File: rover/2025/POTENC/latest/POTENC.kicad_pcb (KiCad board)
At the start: 4 copper layers, 20 x 23.1 mm, 4 parts, among them J1 POT, J2 Conn_01x06_Socket, J3 RJ50-SS-641010-A-NF-A111

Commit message: ARM-JL REV0 done
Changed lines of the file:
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@@
 	)
 	(segment
-		(start 54.28766 38.84)
-		(end 54.40766 38.84)
-		(width 0.1565)
-		(layer "F.Cu")
-		(net 5)
-	)
-	(segment
-		(start 54.04766 38.428531)
-		(end 54.04766 38.6)
-		(width 0.1565)
-		(layer "F.Cu")
-		(net 5)
-	)
-	(segment
-		(start 56.778149 38.84)
-		(end 56.901 38.84)
-		(width 0.1565)
-		(layer "F.Cu")
-		(net 5)
-	)
-	(segment
-		(start 53.68766 38.188531)
-		(end 53.80766 38.188531)
+		(start 54.432799 38.84)
+		(end 55.237661 38.84)
+		(width 0.1565)
+		(layer "F.Cu")
+		(net 5)
+	)
+	(segment
+		(start 49.881 38.84)
+		(end 53.232799 38.84)
 		(width 0.1565)
 		(layer "F.Cu")
@@
 	)
 	(segment
-		(start 54.40766 38.84)
-		(end 56.778149 38.84)
-		(width 0.1565)
-		(layer "F.Cu")
-		(net 5)
-	)
-	(segment
-		(start 53.44766 38.6)
-		(end 53.44766 38.428531)
-		(width 0.1565)
-		(layer "F.Cu")
-		(net 5)
-	)
-	(segment
-		(start 49.881 38.84)
-		(end 53.20766 38.84)
-		(width 0.1565)
-		(layer "F.Cu")
-		(net 5)
-	)
-	(arc
-		(start 53.80766 38.188531)
-		(mid 53.977366 38.258825)
-		(end 54.04766 38.428531)
-		(width 0.1565)
-		(layer "F.Cu")
-		(net 5)
-	)
-	(arc
-		(start 53.44766 38.428531)
-		(mid 53.517954 38.258825)
-		(end 53.68766 38.188531)
-		(width 0.1565)
-		(layer "F.Cu")
-		(net 5)
-	)
-	(arc
-		(start 54.04766 38.6)
-		(mid 54.117954 38.769706)
-		(end 54.28766 38.84)
-		(width 0.1565)
-		(layer "F.Cu")
-		(net 5)
-	)
-	(arc
-		(start 53.20766 38.84)
-		(mid 53.377366 38.769706)
-		(end 53.44766 38.6)
+		(start 55.237661 38.84)
+		(end 56.901 38.84)
+		(width 0.1565)
+		(layer "F.Cu")
+		(net 5)
+	)
+	(segment
+		(start 53.712799 38.188452)
+		(end 53.832799 38.188452)
+		(width 0.1565)
+		(layer "F.Cu")
+		(net 5)
+	)
+	(segment
+		(start 53.472799 38.6)
+		(end 53.472799 38.428452)
+		(width 0.1565)
+		(layer "F.Cu")
+		(net 5)
+	)
+	(segment
+		(start 54.072799 38.428452)
+		(end 54.072799 38.6)
+		(width 0.1565)
+		(layer "F.Cu")
+		(net 5)
+	)
+	(segment
+		(start 54.312799 38.84)
+		(end 54.432799 38.84)
+		(width 0.1565)
+		(layer "F.Cu")
+		(net 5)
+	)
+	(arc
+		(start 53.232799 38.84)
+		(mid 53.402505 38.769706)
+		(end 53.472799 38.6)
+		(width 0.1565)
+		(layer "F.Cu")
+		(net 5)
+	)
+	(arc
+		(start 53.472799 38.428452)
+		(mid 53.543093 38.258746)
+		(end 53.712799 38.188452)
+		(width 0.1565)
+		(layer "F.Cu")
+		(net 5)
+	)
+	(arc
+		(start 54.072799 38.6)
+		(mid 54.143093 38.769706)
+		(end 54.312799 38.84)
+		(width 0.1565)
+		(layer "F.Cu")
+		(net 5)
+	)
+	(arc
+		(start 53.832799 38.188452)
+		(mid 54.002505 38.258746)
+		(end 54.072799 38.428452)
 		(width 0.1565)
 		(layer "F.Cu")
@@
 		(base_line
 			(pts
-				(xy 53.20766 38.84) (xy 56.778149 38.84)
+				(xy 53.232799 38.84) (xy 55.237661 38.84)
 			)
 		)
 		(corner_radius_percent 80)
 		(end
-			(xy 56.778149 38.84)
+			(xy 55.237661 38.84)
 		)
 		(initial_side "left")
@@
 		(min_spacing 0.6)
 		(origin
-			(xy 53.20766 38.84)
+			(xy 53.232799 38.84)
 		)
 		(override_custom_rules no)
@@
 		(target_skew_min -0.1)
 		(tuning_mode "single")
-		(members 08646f17-06fd-4c29-ab54-9f907d7e007d 23642393-6d20-4e0a-a633-02d655d8fe32
-			50fe9728-9544-4e31-9ede-62f20ce672bc 7a298e16-b502-4518-ac2e-b2232d07230b
-			7cae2099-89ad-4c9e-b411-a0003c0e390b 7faa5dc3-3f2f-4b30-982f-42c6eebeb8f4
-			ba017a85-c32f-4e7a-8ff5-d6a4cad0f463 cb7169b9-30f8-433c-bf78-d530e59199b3
-			dc584919-7d87-47ae-8067-9ec3da415911
-		)
-	)
+		(members 11f3ff64-4542-4d84-bcd1-c042a52550a3 5cca4dc9-0e20-4a9f-ad20-37a15c82bc22
+			600dcb4f-a10e-41ee-a665-fec5106fd8ec 625a1d7f-7c46-4d6e-a7c7-2fe0f5ee1ae3
+			722e51ba-4d99-4d38-9a8b-174001b387e3 7dfdbcde-aa8e-4f0b-9cdf-393ebc9b7516
+			8eb33b44-b72d-49b2-8921-c9b8324203fd aa7d440b-d345-45c7-9ee1-a23ab4ce170f
+			dfb8d912-b477-43f9-b57d-55b74f0db737
+		)
+	)

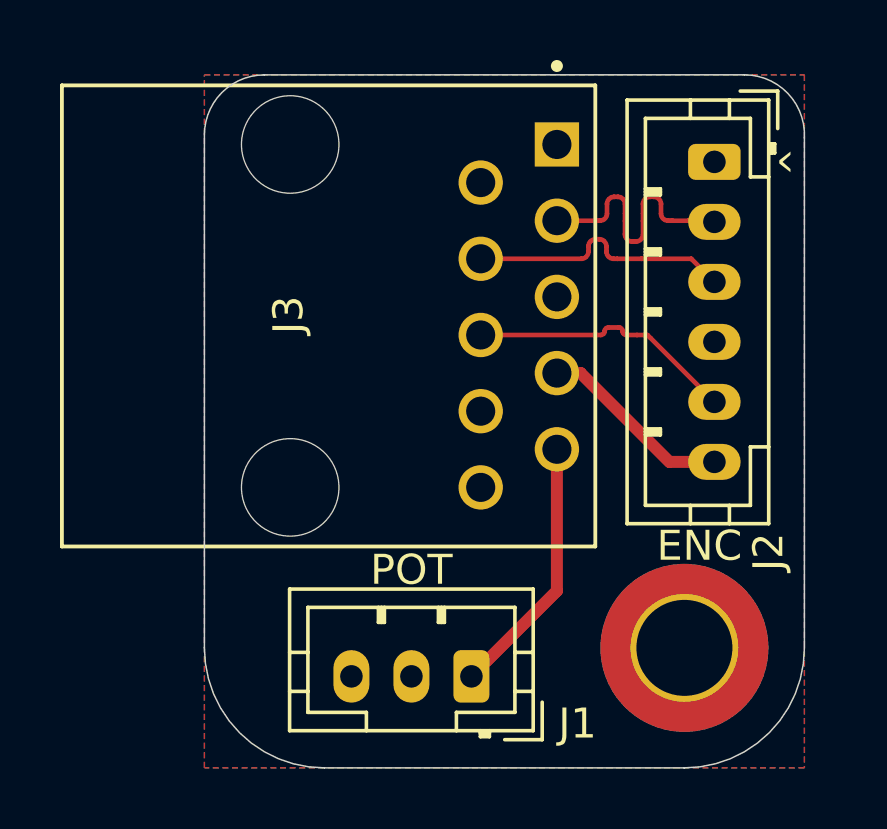
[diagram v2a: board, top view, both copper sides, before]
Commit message: ArmJ2 revised for order
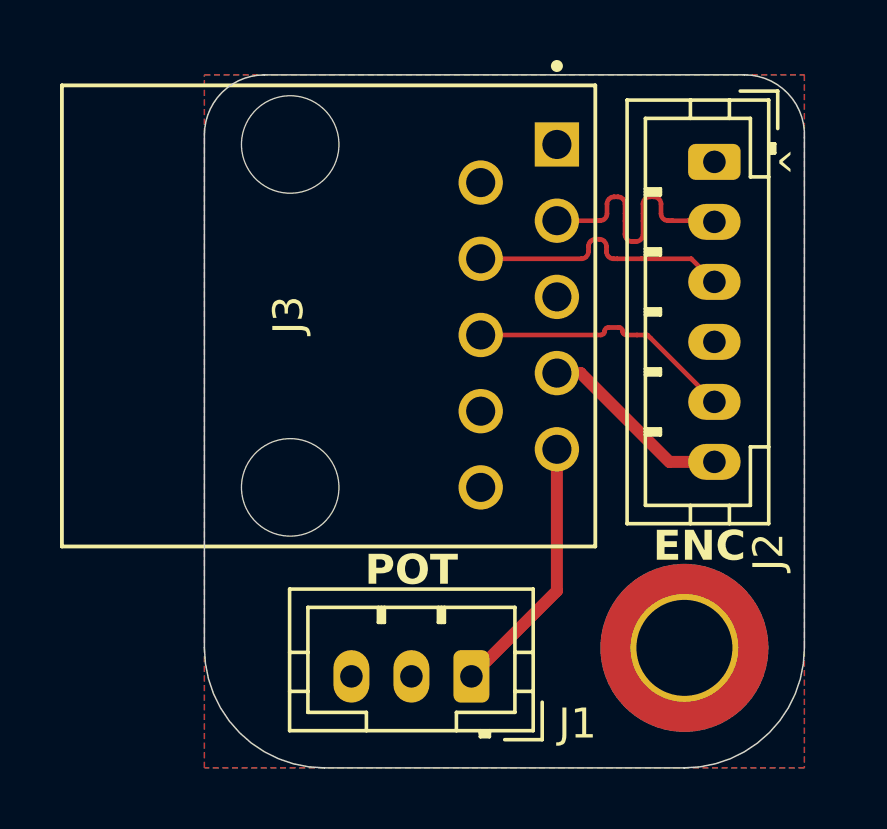
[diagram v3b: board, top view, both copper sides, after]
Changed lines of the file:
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@@
 		)
 		(property "Value" "POT"
-			(at 2 4 0)
-			(layer "F.Fab")
+			(at 1.8 5.35 0)
+			(layer "F.Fab")
+			(hide yes)
 			(effects
 				(font
@@
 			(font
 				(size 1 0.8)
-				(thickness 0.1)
+				(thickness 0.16)
+				(bold yes)
 			)
 			(justify mirror)
@@
 			(font
 				(size 1 0.8)
-				(thickness 0.1)
+				(thickness 0.16)
+				(bold yes)
 			)
 			(justify left mirror)
@@
 			(font
 				(size 1 0.8)
-				(thickness 0.1)
+				(thickness 0.16)
+				(bold yes)
 			)
 			(justify left mirror)
@@
 			(font
 				(size 1 0.8)
-				(thickness 0.1)
+				(thickness 0.16)
+				(bold yes)
 			)
 			(justify left mirror)
@@
 			(font
 				(size 1 0.8)
-				(thickness 0.1)
+				(thickness 0.16)
+				(bold yes)
 			)
 			(justify left mirror)
@@
 			(font
 				(size 1 0.8)
-				(thickness 0.1)
+				(thickness 0.16)
+				(bold yes)
 			)
 			(justify right mirror)
@@
 			(font
 				(size 1 0.8)
-				(thickness 0.1)
+				(thickness 0.16)
+				(bold yes)
 			)
 			(justify right mirror)
@@
 			(font
 				(size 1 0.8)
-				(thickness 0.1)
+				(thickness 0.16)
+				(bold yes)
 			)
 			(justify mirror)
@@
 			(font
 				(size 1 0.8)
-				(thickness 0.1)
+				(thickness 0.16)
+				(bold yes)
 			)
 			(justify right mirror)
@@
 			(font
 				(size 1 0.8)
-				(thickness 0.1)
+				(thickness 0.16)
+				(bold yes)
 			)
 			(justify mirror)
@@
 			(font
 				(size 1 0.8)
-				(thickness 0.1)
+				(thickness 0.16)
+				(bold yes)
 			)
 			(justify left mirror)
@@
 			(font
 				(size 1 0.8)
-				(thickness 0.1)
+				(thickness 0.16)
+				(bold yes)
 			)
 			(justify right mirror)
@@
 			(font
 				(size 1 0.8)
-				(thickness 0.1)
+				(thickness 0.16)
+				(bold yes)
 			)
 			(justify mirror)
@@
 			(font
 				(size 1 1)
-				(thickness 0.1)
+				(thickness 0.2)
+				(bold yes)
 			)
 		)
@@
 			(font
 				(size 1 1)
-				(thickness 0.1)
-			)
-		)
+				(thickness 0.2)
+				(bold yes)
+			)
+		)
